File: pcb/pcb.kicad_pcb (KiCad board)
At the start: 2 copper layers, 75 x 75 mm, 33 parts, among them J1 Connector, USB-TYPE-C-16P, U2 W25Q16JVSS, U4 NCP1117-3.3_SOT223, X1 X322512MSB4SI

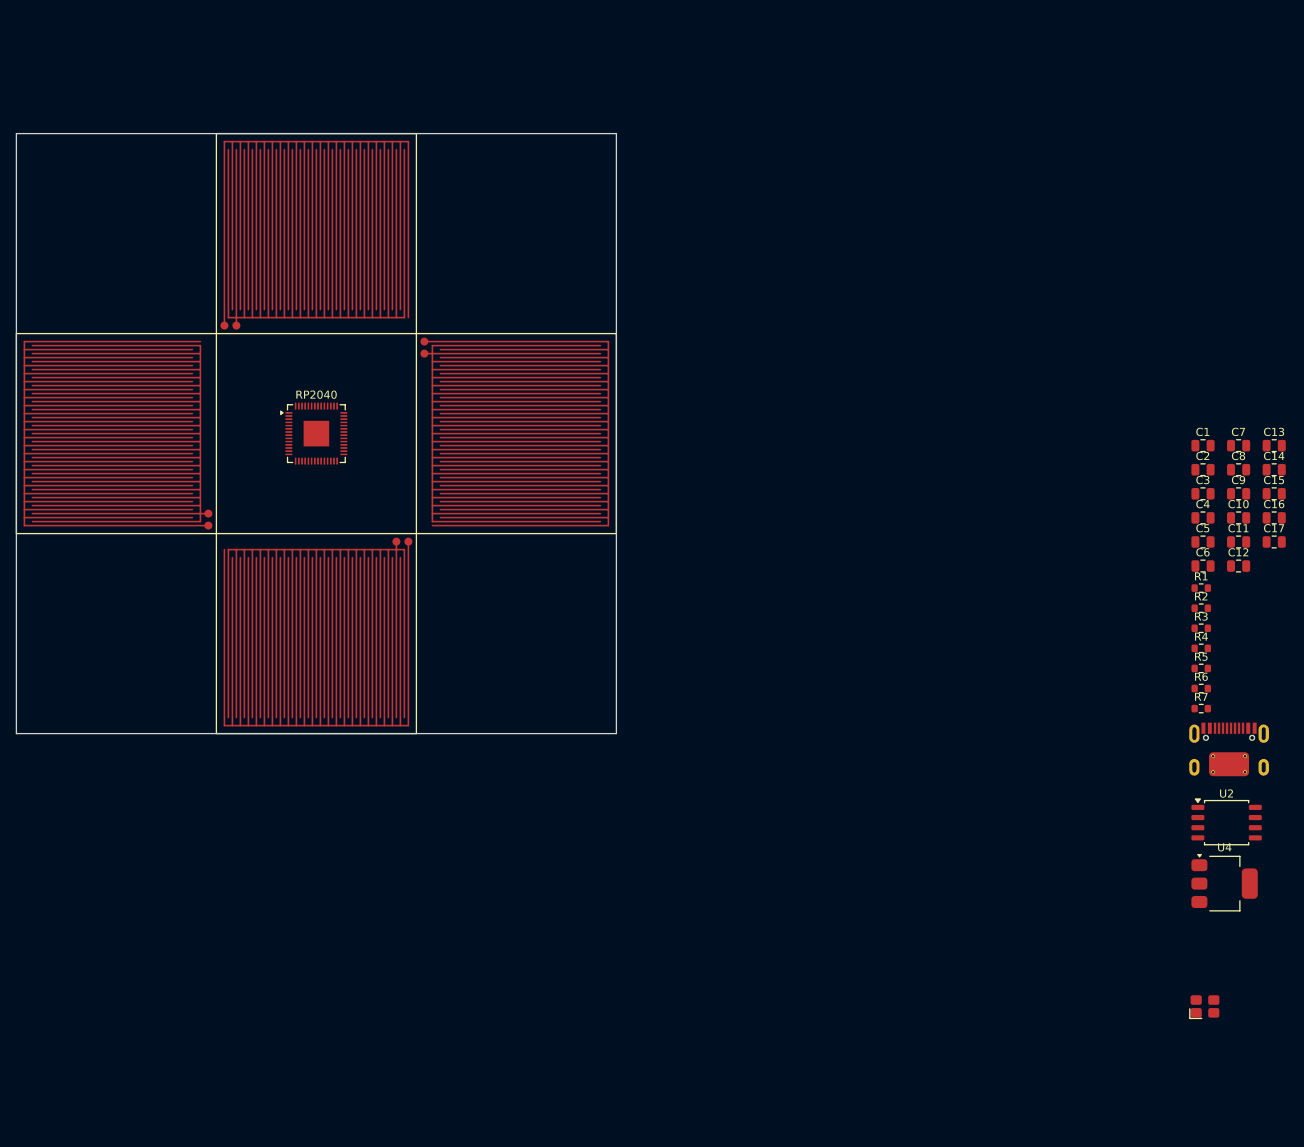
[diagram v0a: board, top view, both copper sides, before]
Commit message: started routing pcb
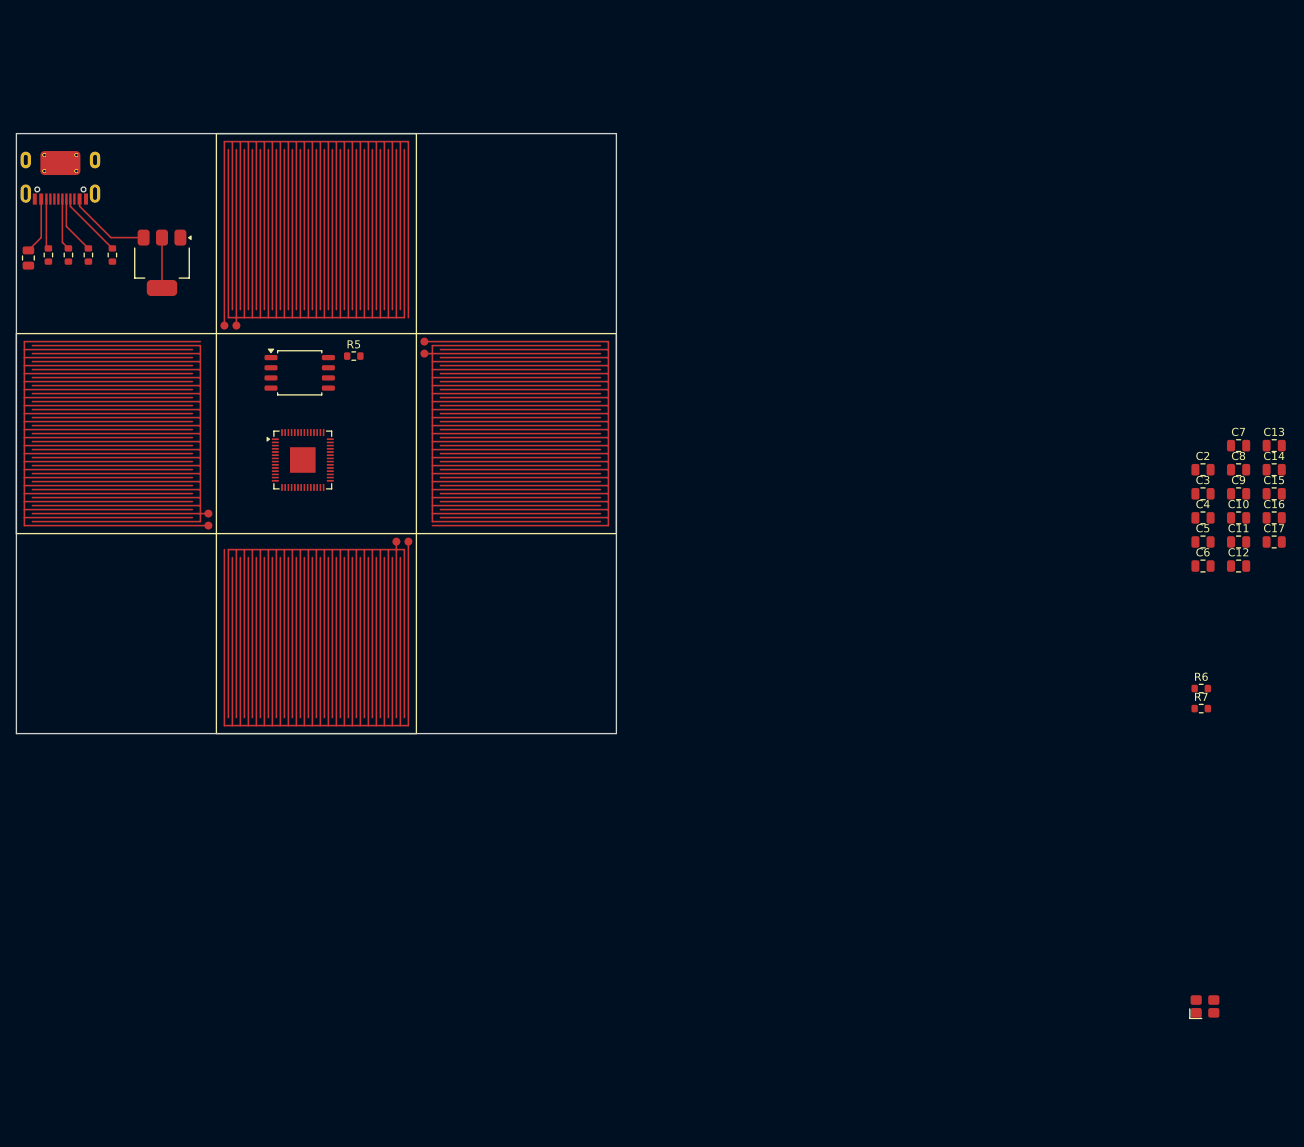
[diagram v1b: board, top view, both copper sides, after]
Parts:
- moved J1 162.5 mm to (5.50, 5.68), turned to 180 degrees
- moved U4 153.8 mm to (18.2, 16.1), turned to -90 degrees
- moved R2 150.7 mm to (4.00, 15.2), turned to 90 degrees
- moved R4 149.9 mm to (6.50, 15.2), turned to 90 degrees
- moved C1 148.7 mm to (1.50, 15.6), turned to -90 degrees
- moved R3 146.7 mm to (9.00, 15.2), turned to 90 degrees
- moved R1 142.3 mm to (12.0, 15.2), turned to -90 degrees
- moved Flash_Storage1 128.8 mm to (35.4, 29.9)
- moved R5 112.9 mm to (42.2, 27.8)
- moved RP2040 3.71 mm to (35.8, 40.8)
- renumbered U2 to Flash_Storage1
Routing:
- net VBUS: track 0.00 -> 17.6 mm
- net Net-(J1-CC1): track 0.00 -> 8.34 mm
- net Net-(J1-D--PadA7): track 0.00 -> 7.31 mm
- net Net-(J1-D+-PadA6): track 0.00 -> 6.48 mm
- net +3V3: track 0.00 -> 6.30 mm
- net Net-(J1-CC2): track 0.00 -> 6.27 mm
- net GND: track 0.00 -> 1.71 mm

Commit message: working on pcb even more
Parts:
- SW_East1, SW_South1: footprint andrews_lib:DDR_PAD_CONTACT -> andrews_lib:DDR_BUTTON_2_M
- SW_North1, SW_West1: footprint andrews_lib:DDR_PAD_CONTACT -> andrews_lib:DDR_BUTTON_2
- moved C1 7.50 mm to (8.78, 13.7)
- moved J1 7.01 mm to (12.5, 6.00)
- moved R2 6.74 mm to (10.5, 13.5)
- moved R4 5.77 mm to (12.0, 13.5)
- moved R3 4.83 mm to (13.5, 13.5)
- moved RP2040 3.71 mm to (37.5, 37.5)
- moved R1 3.46 mm to (15.0, 13.5)
- moved U4 1.23 mm to (19.4, 16.4)
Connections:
- Flash_Storage1 pad 4: unconnected-(Flash_Storage1-GND-Pad4) -> GND
- RP2040 pad 57: unconnected-(RP2040-GND-Pad57) -> GND
- RP2040 pad 6: unconnected-(RP2040-GPIO4-Pad6) -> GPIO_04
- RP2040 pad 7: unconnected-(RP2040-GPIO5-Pad7) -> GPIO_05
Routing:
- net GND: track 1.71 -> 37.5 mm
- net VBUS: track 17.6 -> 10.5 mm
- net Net-(J1-CC1): track 8.34 -> 4.70 mm
- net Net-(J1-D--PadA7): track 7.31 -> 4.29 mm
- net Net-(J1-D+-PadA6): track 6.48 -> 4.29 mm
- net Net-(J1-CC2): track 6.27 -> 4.27 mm

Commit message: working on pcb even more
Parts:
- added SW1: SW_Push, andrews_lib:Tactile_Switch_4.2x3.2, F.Cu at (67.8, 61.2)
- added SW_Menu1: SW_Push, andrews_lib:Tactile_Switch_4.2x3.2, F.Cu at (58.5, 5.00)
- added SW_Start1: SW_Push, andrews_lib:Tactile_Switch_4.2x3.2, F.Cu at (66.5, 5.00)
- moved X1 136.0 mm to (30.5, 41.5)
- moved C2 130.4 mm to (21.6, 11.0)
- moved C16 127.3 mm to (30.2, 38.8)
- moved C17 126.9 mm to (30.4, 45.7), turned to 180 degrees
- moved R7 121.2 mm to (30.2, 44.0)
- moved C4 118.3 mm to (30.0, 49.5), turned to -90 degrees
- moved C7 117.2 mm to (36.0, 49.5), turned to -90 degrees
- moved C5 116.3 mm to (32.0, 49.5), turned to -90 degrees
- moved C8 115.0 mm to (38.0, 49.5), turned to -90 degrees
- moved C6 114.4 mm to (34.0, 49.5), turned to -90 degrees
- moved C13 113.5 mm to (44.0, 46.0)
- moved C15 113.3 mm to (44.0, 42.0)
- moved C14 113.3 mm to (44.0, 44.0)
- moved C9 112.9 mm to (40.0, 49.5), turned to -90 degrees
- moved C10 110.8 mm to (42.0, 49.5), turned to -90 degrees
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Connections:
- SW_North1 pad 2: GPIO_01 -> GPIO_03
- SW_South1 pad 2: GPIO_03 -> GPIO_05
- SW_West1 pad 2: GPIO_02 -> GPIO_04
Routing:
- net GPIO_01: track 0.00 -> 42.9 mm
- net QSPI_SD1: track 0.00 -> 36.2 mm
- net GPIO_02: track 0.00 -> 35.4 mm
- net QSPI_SD2: track 0.00 -> 34.0 mm
- net GPIO_05: track 0.00 -> 32.0 mm
- net GND: track 37.5 -> 6.65 mm, vias 0 -> 2
- net QSPI_SD3: track 0.00 -> 30.0 mm
- net +3V3: track 6.30 -> 35.8 mm
- net QSPI_SCLK: track 0.00 -> 29.2 mm
- net QSPI_SD0: track 0.00 -> 27.9 mm
- net GPIO_04: track 0.00 -> 22.2 mm
- net GPIO_00: track 0.00 -> 18.3 mm
- net GPIO_03: track 0.00 -> 15.6 mm
- net XOUT: track 0.00 -> 8.82 mm
- net XIN: track 0.00 -> 7.52 mm
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- added copper zone on F.Cu, net GND

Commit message: work on it yay
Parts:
- SW1, SW_Menu1, SW_Start1: footprint andrews_lib:Tactile_Switch_4.2x3.2 -> Andrews_Library:Tactile_Switch_4.2x3.2
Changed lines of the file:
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@@
 		(sheetname "/")
 		(sheetfile "pcb.kicad_sch")
+		(units
+			(unit
+				(name "A")
+				(pins "1" "2")
+			)
+		)
 		(attr smd)
 		(duplicate_pad_numbers_are_jumpers no)
@@
 		)
 	)
-	(footprint "andrews_lib:Tactile_Switch_4.2x3.2"
+	(footprint "Andrews_Library:Tactile_Switch_4.2x3.2"
 		(layer "F.Cu")
 		(at 67.75 61.175 180)
 		(property "Reference" "SW1"
-			(at 0 0 180)
+			(at -15 -12.5 180)
 			(unlocked yes)
 			(layer "F.SilkS")
-			(hide yes)
 			(effects
 				(font
-					(size 0.5 1)
+					(size 1 1)
 					(thickness 0.1)
 				)
@@
 		)
 		(property "Value" "SW_Push"
-			(at 0 3 180)
+			(at -15 -11 180)
 			(unlocked yes)
 			(layer "F.Fab")
-			(hide yes)
 			(effects
 				(font
@@
 		(sheetname "/")
 		(sheetfile "pcb.kicad_sch")
-		(units
-			(unit
-				(name "A")
-				(pins "1" "2")
-			)
-		)
 		(attr smd)
 		(duplicate_pad_numbers_are_jumpers no)
@@
 			(stroke
 				(width 0.1)
-				(type default)
+				(type solid)
 			)
 			(layer "F.SilkS")
 		)
 		(fp_text user "${REFERENCE}"
-			(at 0 0 180)
+			(at -15 -9.5 180)
 			(unlocked yes)
 			(layer "F.Fab")
@@
 			(pintype "passive")
 		)
-		(pad "2" smd rect
+		(pad "2" smd roundrect
 			(at 2.25 -1.075 180)
 			(size 1 0.7)
 			(layers "F.Cu" "F.Mask" "F.Paste")
+			(roundrect_rratio 0.15)
 			(net "Net-(R6-Pad1)")
 			(pinfunction "2_2")
@@
 			(layers "F.Cu" "F.Mask" "F.Paste")
 		)
-		(pad "4" smd rect
+		(pad "4" smd roundrect
 			(at 2.25 1.075 180)
 			(size 1 0.7)
 			(layers "F.Cu" "F.Mask" "F.Paste")
+			(roundrect_rratio 0.15)
 		)
 		(zone
-			(layer "F.CrtYd")
+			(layer "F.SilkS")
 			(hatch edge 0.5)
 			(connect_pads
@@
 		)
 		(embedded_fonts no)
-		(model "${KIPRJMOD}/andrews_lib.pretty/Tactile_Switch_4.2x3.2.step"
+		(model "${KIPRJMOD}/Tactile_Switch_4.2x3.2.step"
 			(offset
 				(xyz 0 0 0)
@@
 		)
 	)
-	(footprint "andrews_lib:Tactile_Switch_4.2x3.2"
+	(footprint "Andrews_Library:Tactile_Switch_4.2x3.2"
 		(layer "F.Cu")
 		(at 66.5 5 -90)
 		(property "Reference" "SW_Start1"
-			(at 0 0 270)
+			(at -15 -12.5 270)
 			(unlocked yes)
 			(layer "F.SilkS")
-			(hide yes)
 			(effects
 				(font
-					(size 0.5 1)
+					(size 1 1)
 					(thickness 0.1)
 				)
@@
 		)
 		(property "Value" "SW_Push"
-			(at 0 3 270)
+			(at -15 -11 270)
 			(unlocked yes)
 			(layer "F.Fab")
-			(hide yes)
 			(effects
 				(font
@@
 		(sheetname "/")
 		(sheetfile "pcb.kicad_sch")
-		(units
-			(unit
-				(name "A")
-				(pins "1" "2")
-			)
-		)
 		(attr smd)
 		(duplicate_pad_numbers_are_jumpers no)
@@
 			(stroke
 				(width 0.1)
-				(type default)
+				(type solid)
 			)
 			(layer "F.SilkS")
 		)
 		(fp_text user "${REFERENCE}"
-			(at 0 0 270)
+			(at -15 -9.5 270)
 			(unlocked yes)
 			(layer "F.Fab")
@@
 			(pintype "passive")
 		)
-		(pad "2" smd rect
+		(pad "2" smd roundrect
 			(at 2.25 -1.075 270)
 			(size 1 0.7)
 			(layers "F.Cu" "F.Mask" "F.Paste")
+			(roundrect_rratio 0.15)
 			(net "GPIO_01")
 			(pinfunction "2_2")
@@
 			(layers "F.Cu" "F.Mask" "F.Paste")
 		)
-		(pad "4" smd rect
+		(pad "4" smd roundrect
 			(at 2.25 1.075 270)
 			(size 1 0.7)
 			(layers "F.Cu" "F.Mask" "F.Paste")
+			(roundrect_rratio 0.15)
 		)
 		(zone
-			(layer "F.CrtYd")
+			(layer "F.SilkS")
 			(hatch edge 0.5)
 			(connect_pads
@@
 		)
 		(embedded_fonts no)
-		(model "${KIPRJMOD}/andrews_lib.pretty/Tactile_Switch_4.2x3.2.step"
+		(model "${KIPRJMOD}/Tactile_Switch_4.2x3.2.step"
 			(offset
 				(xyz 0 0 0)
@@
 		(sheetname "/")
 		(sheetfile "pcb.kicad_sch")
+		(units
+			(unit
+				(name "A")
+				(pins "1" "2")
+			)
+		)
 		(attr smd)
 		(duplicate_pad_numbers_are_jumpers no)
@@
 		(sheetname "/")
 		(sheetfile "pcb.kicad_sch")
+		(units
+			(unit
+				(name "A")
+				(pins "1" "2")
+			)
+		)
 		(attr smd)
 		(duplicate_pad_numbers_are_jumpers no)
@@
 		)
 	)
-	(footprint "andrews_lib:Tactile_Switch_4.2x3.2"
+	(footprint "Andrews_Library:Tactile_Switch_4.2x3.2"
 		(layer "F.Cu")
 		(at 58.5 5 -90)
 		(property "Reference" "SW_Menu1"
-			(at 0 0 270)
+			(at -15 -12.5 270)
 			(unlocked yes)
 			(layer "F.SilkS")
-			(hide yes)
 			(effects
 				(font
-					(size 0.5 1)
+					(size 1 1)
 					(thickness 0.1)
 				)
@@
 		)
 		(property "Value" "SW_Push"
-			(at 0 3 270)
+			(at -15 -11 270)
 			(unlocked yes)
 			(layer "F.Fab")
-			(hide yes)
 			(effects
 				(font
@@
 		(sheetname "/")
 		(sheetfile "pcb.kicad_sch")
-		(units
-			(unit
-				(name "A")
-				(pins "1" "2")
-			)
-		)
 		(attr smd)
 		(duplicate_pad_numbers_are_jumpers no)
@@
 			(stroke
 				(width 0.1)
-				(type default)
+				(type solid)
 			)
 			(layer "F.SilkS")
 		)
 		(fp_text user "${REFERENCE}"
-			(at 0 0 270)
+			(at -15 -9.5 270)
 			(unlocked yes)
 			(layer "F.Fab")
@@
 			(pintype "passive")
 		)
-		(pad "2" smd rect
+		(pad "2" smd roundrect
 			(at 2.25 -1.075 270)
 			(size 1 0.7)
 			(layers "F.Cu" "F.Mask" "F.Paste")
+			(roundrect_rratio 0.15)
 			(net "GPIO_02")
 			(pinfunction "2_2")
@@
 			(layers "F.Cu" "F.Mask" "F.Paste")
 		)
-		(pad "4" smd rect
+		(pad "4" smd roundrect
 			(at 2.25 1.075 270)
 			(size 1 0.7)
 			(layers "F.Cu" "F.Mask" "F.Paste")
+			(roundrect_rratio 0.15)
 		)
 		(zone
-			(layer "F.CrtYd")
+			(layer "F.SilkS")
 			(hatch edge 0.5)
 			(connect_pads
@@
 		)
 		(embedded_fonts no)
-		(model "${KIPRJMOD}/andrews_lib.pretty/Tactile_Switch_4.2x3.2.step"
+		(model "${KIPRJMOD}/Tactile_Switch_4.2x3.2.step"
 			(offset
 				(xyz 0 0 0)
@@
 		(sheetname "/")
 		(sheetfile "pcb.kicad_sch")
+		(units
+			(unit
+				(name "A")
+				(pins "1" "2")
+			)
+		)
 		(attr smd)
 		(duplicate_pad_numbers_are_jumpers no)

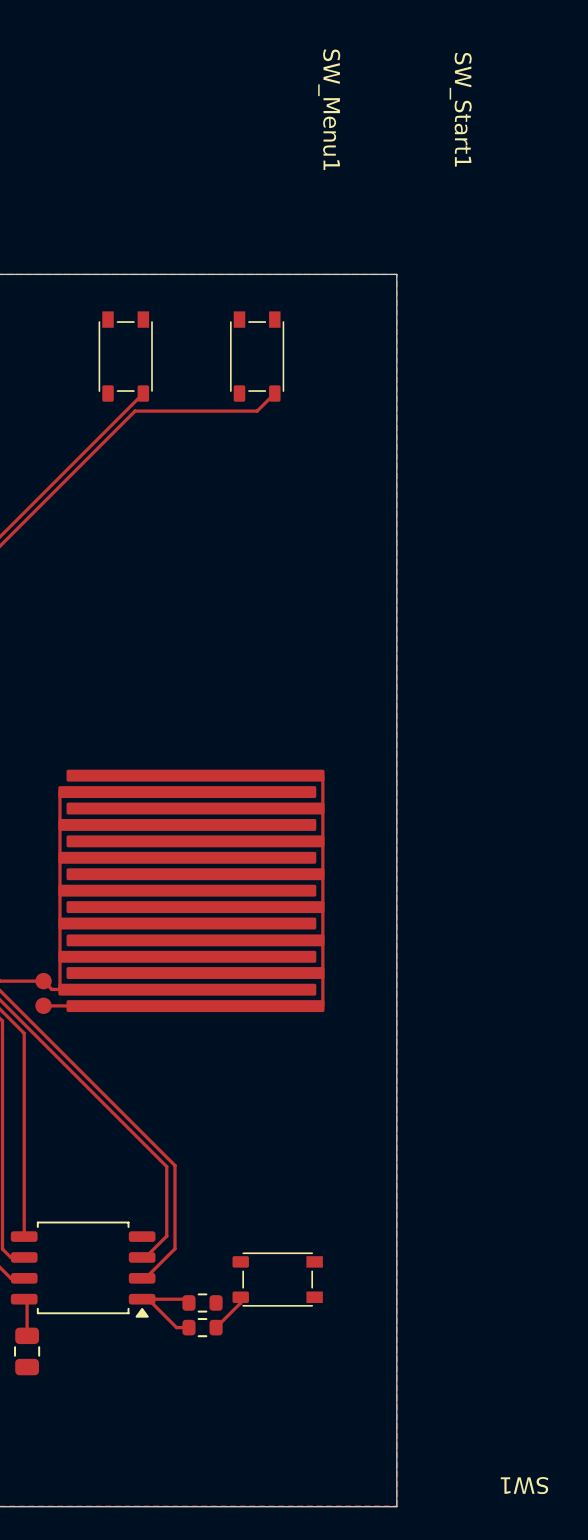
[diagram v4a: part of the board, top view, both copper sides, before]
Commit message: buttons on pcb
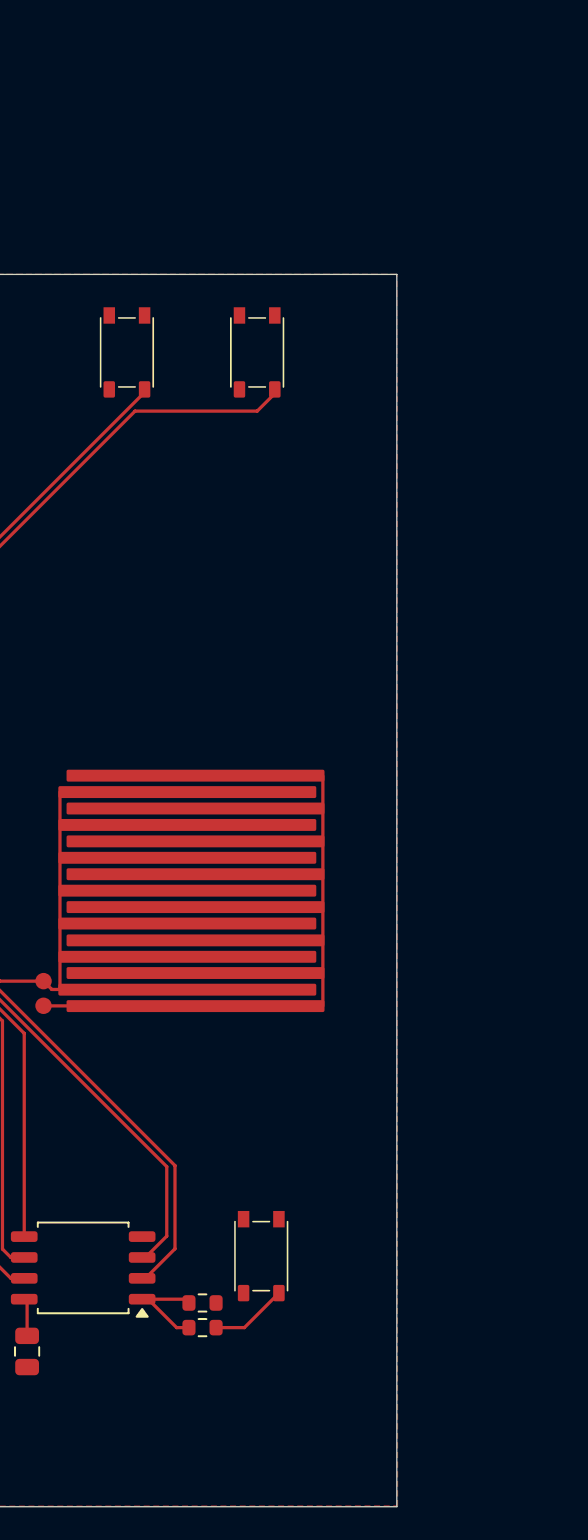
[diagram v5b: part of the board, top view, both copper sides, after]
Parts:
- moved SW1 1.74 mm to (66.8, 59.8), turned to -90 degrees
- moved SW_Menu1 0.26 mm to (58.6, 4.75)
- moved SW_Start1 0.25 mm to (66.5, 4.75)
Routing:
- net Net-(R6-Pad1): track 2.47 -> 4.69 mm

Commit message: more schematic work
grounds are gay :(
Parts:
- moved C13 6.32 mm to (37.8, 44.8), turned to -90 degrees
- moved C14 4.28 mm to (39.8, 44.8), turned to -90 degrees
- moved C15 3.56 mm to (41.8, 44.8), turned to -90 degrees
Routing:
- net +3V3: track 35.8 -> 228.7 mm
- net USB_D+: track 0.00 -> 130.9 mm
- net USB_D-: track 0.00 -> 129.3 mm
- net QSPI_SS: track 6.51 -> 44.8 mm
- net GND: track 6.65 -> 29.0 mm
- net +1V1: track 6.85 -> 11.6 mm
- net GPIO_00: track 18.3 -> 19.2 mm

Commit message: still working on it LOL
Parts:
- moved C17 90.7 mm to (106.2, 95.4)
- moved R5 90.7 mm to (139.0, 112.2)
- moved R6 90.7 mm to (139.0, 113.8)
- moved R7 90.7 mm to (106.0, 93.6)
- moved SW_Menu1 90.7 mm to (134.4, 54.4)
- moved C1 90.7 mm to (84.6, 63.4)
- moved C10 90.7 mm to (117.8, 99.2)
- moved C11 90.7 mm to (119.8, 99.2)
- moved C12 90.7 mm to (121.8, 99.2)
- moved C13 90.7 mm to (113.6, 94.5)
- moved C14 90.7 mm to (115.6, 94.5)
- moved C15 90.7 mm to (117.6, 94.5)
- moved C16 90.7 mm to (106.1, 88.4)
- moved C2 90.7 mm to (97.5, 60.6)
- moved C3 90.7 mm to (128.3, 115.2)
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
